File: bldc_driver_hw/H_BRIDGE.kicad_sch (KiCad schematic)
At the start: 21 parts, among them Q1 IPB026N06NATMA1, Q3 IPB026N06NATMA1

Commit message: wip
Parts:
- removed R25, R51: SHUNT, symbol Device:R_Small
- added R65, R68: 30m, Resistor_SMD:R_2512_6332Metric, symbol Device:R_Small
- D4, D9: footprint (none) -> Diode_SMD:D_SMB
- R18, R19, R20, R21, R22, R26, R27, R28: footprint (none) -> Resistor_SMD:R_0805_2012Metric
- R54: value SHUNT -> 30m; footprint (none) -> Resistor_SMD:R_2512_6332Metric
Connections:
- net PHASE: now also R65.2, R68.2
- net SHUNT_P: now also R65.1, R68.1

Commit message: schematic finished pcb in progress
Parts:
- C51: renamed from C25; footprint Capacitor_SMD:C_0805_2012Metric_Pad1.18x1.45mm_HandSolder -> Capacitor_SMD:C_0805_2012Metric
- C52: renamed from C26; footprint Capacitor_SMD:C_0805_2012Metric_Pad1.18x1.45mm_HandSolder -> Capacitor_SMD:C_0805_2012Metric
- R42: renamed from R26; value C_snub -> R_SNUB
- TP30: renamed from TP4; footprint (none) -> TestPoint:TestPoint_Pad_D2.0mm
- TP31: renamed from TP5; footprint (none) -> TestPoint:TestPoint_Pad_D2.0mm
- renumbered D9 to D10, D11 to D7, D16 to D8, D4 to D9, Q3 to Q2, R28 to R33, R18 to R34, R19 to R35, R20 to R36, R21 to R37, R22 to R38, R54 to R39, R65 to R40, R68 to R41, R27 to R43

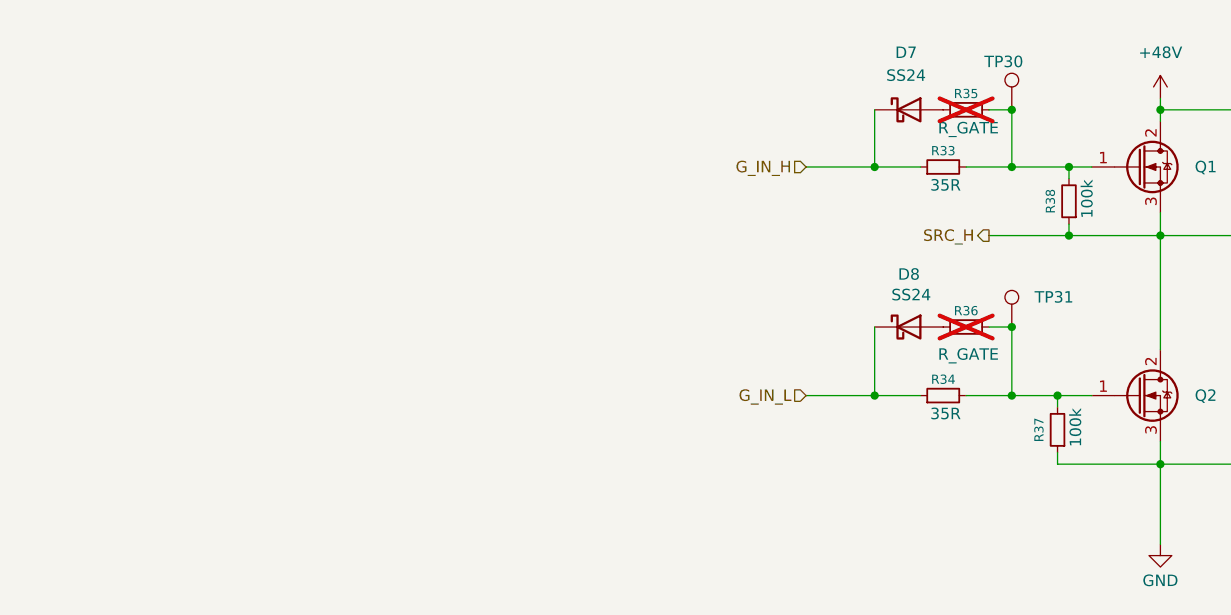
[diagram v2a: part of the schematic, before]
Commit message: Changed one 3 phase driver to three h-bridges and changed buck converter which sink more current
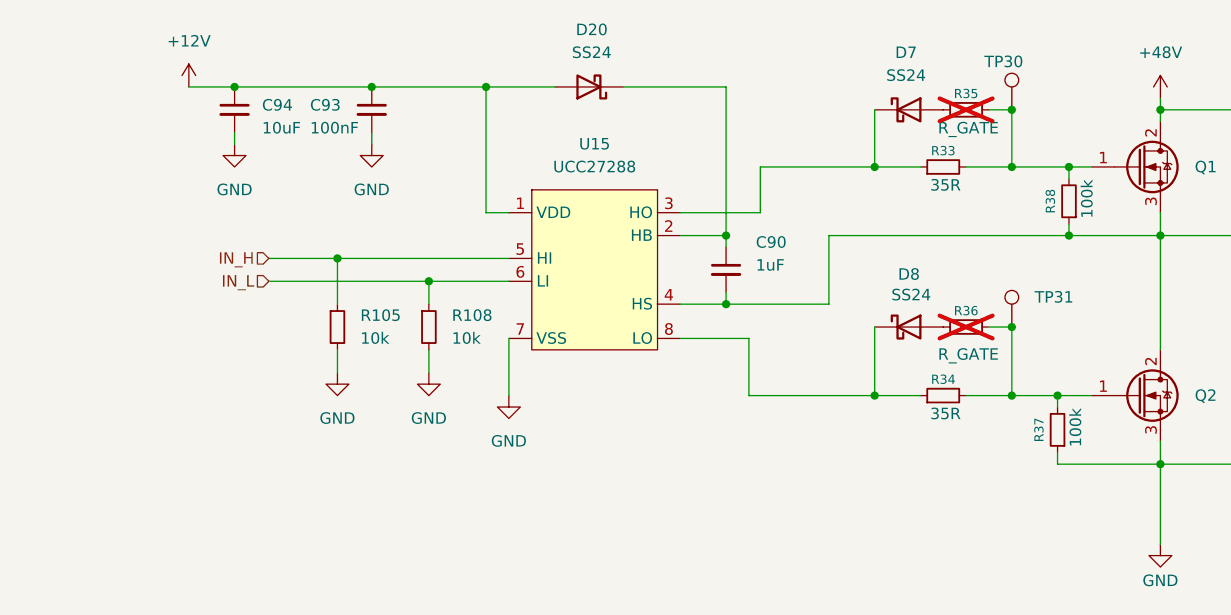
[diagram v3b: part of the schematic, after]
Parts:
- added C90: 1uF, Capacitor_SMD:C_0603_1608Metric, symbol Device:C_Small
- added C93: 100nF, Capacitor_SMD:C_0603_1608Metric, symbol Device:C_Small
- added C94: 10uF, Capacitor_SMD:C_0603_1608Metric, symbol Device:C_Small
- added D20: SS24, Diode_SMD:D_SMA, symbol Diode:SS24
- added R105, R108: 10k, Resistor_SMD:R_0603_1608Metric, symbol Device:R_Small
- added U15: UCC27288, Package_SO:SOIC-8_3.9x4.9mm_P1.27mm, symbol bldc_driver_lib:UCC27288
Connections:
- net GND: now also C93.2, C94.2, R105.2, R108.2, U15.7 (VSS)
- net SHUNT_P: now also C90.2, U15.4 (HS)
- net G_IN_H: no longer names the net of D7.1 (K), R33.1
- net G_IN_H: now also U15.3 (HO)
- net G_IN_L: no longer names the net of D8.1 (K), R34.1
- net G_IN_L: now also U15.8 (LO)
- new net: C90.1, D20.1 (K), U15.2 (HB)
- new net +12V: C93.1, C94.1, D20.2 (A), U15.1 (VDD)
- new net IN_H: R105.1, U15.5 (HI)
- new net IN_L: R108.1, U15.6 (LI)

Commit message: Board finished to review
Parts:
- C51, C52: footprint Capacitor_SMD:C_0805_2012Metric -> Capacitor_SMD:C_1206_3216Metric
- R42: footprint Resistor_SMD:R_0805_2012Metric -> Resistor_SMD:R_1206_3216Metric
- R43: value R_snub -> R_SNUB; footprint Resistor_SMD:R_0805_2012Metric -> Resistor_SMD:R_1206_3216Metric

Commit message: board finished
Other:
- note removed: "Filter: https://www.st.com/resource/en/application_note/an4304-how-to-filter-the-input-of-a-highside-current-sensing-stmicroelectronics.pdf"
- note removed: "https://e2e.ti.com/support/motor-drivers-group/motor-drivers/f/motor-drivers-forum/991693/faq-proper-rc-snubber-design-for-motor-drivers"
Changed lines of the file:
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@@
-		)
-	)
-	(text "https://e2e.ti.com/support/motor-drivers-group/motor-drivers/f/motor-drivers-forum/991693/faq-proper-rc-snubber-design-for-motor-drivers"
-		(exclude_from_sim no)
-		(at 92.964 174.498 0)
-		(effects
-			(font
-				(size 1.27 1.27)
-			)
-		)
-	)
-	(text "Filter:\nhttps://www.st.com/resource/en/application_note/an4304-how-to-filter-the-input-of-a-highside-current-sensing-stmicroelectronics.pdf"
-		(exclude_from_sim no)
-		(at 89.154 182.372 0)
-		(effects
-			(font
-				(size 1.27 1.27)
-			)
 		)
 	)

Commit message: added lcsc codes
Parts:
- C90: LCSC (none) -> C15849; Rating 50V -> (none)
- C93: LCSC (none) -> C14663
- C94: LCSC (none) -> C96446
- D20, D7, D8: value SS24 -> SS54; LCSC (none) -> C22452
- R105, R108: LCSC (none) -> C25804
- R33, R34: value 35R -> 33R; LCSC (none) -> C17634
- R35, R36: value R_GATE -> 0R; LCSC (none) -> C15402; now fitted
- R37, R38: LCSC (none) -> C25803
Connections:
- net at R35.1: now also Q1.1 (G), R33.2, R38.2, TP30.1; no longer D7.2 (A)
- new net: D7.2 (A), R35.2

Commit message: finished_board
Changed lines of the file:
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@@
 		)
 		(property "LCSC" "C15402"
-			(at 116.84 48.26 0)
-			(effects
-				(font
-					(size 1.27 1.27)
-				)
+			(at 116.332 40.132 90)
+			(effects
+				(font
+					(size 1.27 1.27)
+				)
+				(hide yes)
 			)
 		)
@@
 		)
 		(property "LCSC" "C15402"
-			(at 116.84 72.39 0)
-			(effects
-				(font
-					(size 1.27 1.27)
-				)
+			(at 113.792 72.644 0)
+			(effects
+				(font
+					(size 1.27 1.27)
+				)
+				(hide yes)
 			)
 		)
@@
 		)
 		(property "LCSC" "C25803"
-			(at 127 83.82 0)
-			(effects
-				(font
-					(size 1.27 1.27)
-				)
+			(at 118.872 85.344 0)
+			(effects
+				(font
+					(size 1.27 1.27)
+				)
+				(hide yes)
 			)
 		)
@@
 					(size 1.27 1.27)
 				)
+				(hide yes)
 			)
 		)
@@
 					(size 1.27 1.27)
 				)
+				(hide yes)
 			)
 		)
@@
 					(size 1.27 1.27)
 				)
+				(hide yes)
 			)
 		)
@@
 					(size 1.27 1.27)
 				)
+				(hide yes)
 			)
 		)
@@
 					(size 1.27 1.27)
 				)
+				(hide yes)
 			)
 		)
@@
 					(size 1.27 1.27)
 				)
+				(hide yes)
 			)
 		)
@@
 					(size 1.27 1.27)
 				)
+				(hide yes)
 			)
 		)
@@
 					(size 1.27 1.27)
 				)
+				(hide yes)
 			)
 		)
@@
 					(size 1.27 1.27)
 				)
+				(hide yes)
 			)
 		)
@@
 					(size 1.27 1.27)
 				)
+				(hide yes)
 			)
 		)
@@
 					(size 1.27 1.27)
 				)
-			)
-		)
+				(hide yes)
+			)
+		)

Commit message: finished
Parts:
- C51, C52, D10, D9, Q1, Q2, R39, R40, R41, R42, R43, TP30, TP31, U15: now left out of the parts list
- R35, R36: LCSC C15402 -> C17477
- R37, R38: LCSC C25803 -> C149504
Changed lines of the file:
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@@
 		(unit 1)
 		(exclude_from_sim no)
-		(in_bom yes)
+		(in_bom no)
 		(on_board yes)
 		(dnp yes)
@@
 			)
 		)
-		(property "LCSC" "C15402"
+		(property "LCSC" "C17477"
 			(at 116.332 40.132 90)
 			(effects
@@
 			)
 		)
-		(property "LCSC" "C15402"
+		(property "LCSC" "C17477"
 			(at 113.792 72.644 0)
 			(effects
@@
 		(unit 1)
 		(exclude_from_sim no)
-		(in_bom yes)
+		(in_bom no)
 		(on_board yes)
 		(dnp yes)
@@
 			)
 		)
-		(property "LCSC" "C25803"
+		(property "LCSC" "C149504"
 			(at 118.872 85.344 0)
 			(effects
@@
 		(unit 1)
 		(exclude_from_sim no)
-		(in_bom yes)
+		(in_bom no)
 		(on_board yes)
 		(dnp no)
@@
 			)
 		)
-		(property "LCSC" "C25803"
+		(property "LCSC" "C149504"
 			(at 128.27 58.42 0)
 			(effects
@@
 		(unit 1)
 		(exclude_from_sim no)
-		(in_bom yes)
+		(in_bom no)
 		(on_board yes)
 		(dnp no)
@@
 		(unit 1)
 		(exclude_from_sim no)
-		(in_bom yes)
+		(in_bom no)
 		(on_board yes)
 		(dnp yes)
@@
 		(unit 1)
 		(exclude_from_sim no)
-		(in_bom yes)
+		(in_bom no)
 		(on_board yes)
 		(dnp no)
@@
 		(unit 1)
 		(exclude_from_sim no)
-		(in_bom yes)
+		(in_bom no)
 		(on_board yes)
 		(dnp no)
@@
 		(unit 1)
 		(exclude_from_sim no)
-		(in_bom yes)
+		(in_bom no)
 		(on_board yes)
 		(dnp no)
@@
 		(unit 1)
 		(exclude_from_sim no)
-		(in_bom yes)
+		(in_bom no)
 		(on_board yes)
 		(dnp no)
@@
 		(unit 1)
 		(exclude_from_sim no)
-		(in_bom yes)
+		(in_bom no)
 		(on_board yes)
 		(dnp yes)
@@
 		(unit 1)
 		(exclude_from_sim no)
-		(in_bom yes)
+		(in_bom no)
 		(on_board yes)
 		(dnp yes)
@@
 		(unit 1)
 		(exclude_from_sim no)
-		(in_bom yes)
+		(in_bom no)
 		(on_board yes)
 		(dnp no)
@@
 		(unit 1)
 		(exclude_from_sim no)
-		(in_bom yes)
+		(in_bom no)
 		(on_board yes)
 		(dnp yes)
@@
 		(unit 1)
 		(exclude_from_sim no)
-		(in_bom yes)
-		(on_board yes)
-		(dnp no)
+		(in_bom no)
+		(on_board yes)
+		(dnp no)
